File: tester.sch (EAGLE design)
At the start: 74 parts, among them IC1 ATmega8/88/168, K1 NA 05W K, M1 SP6000C-180, P1 250, P2 10k lin, Q1 BC847CSMD, Q2 BC847CSMD, Q3 BC807-40SMD, Q4 8,000 MHz, Q5 BC847CSMD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

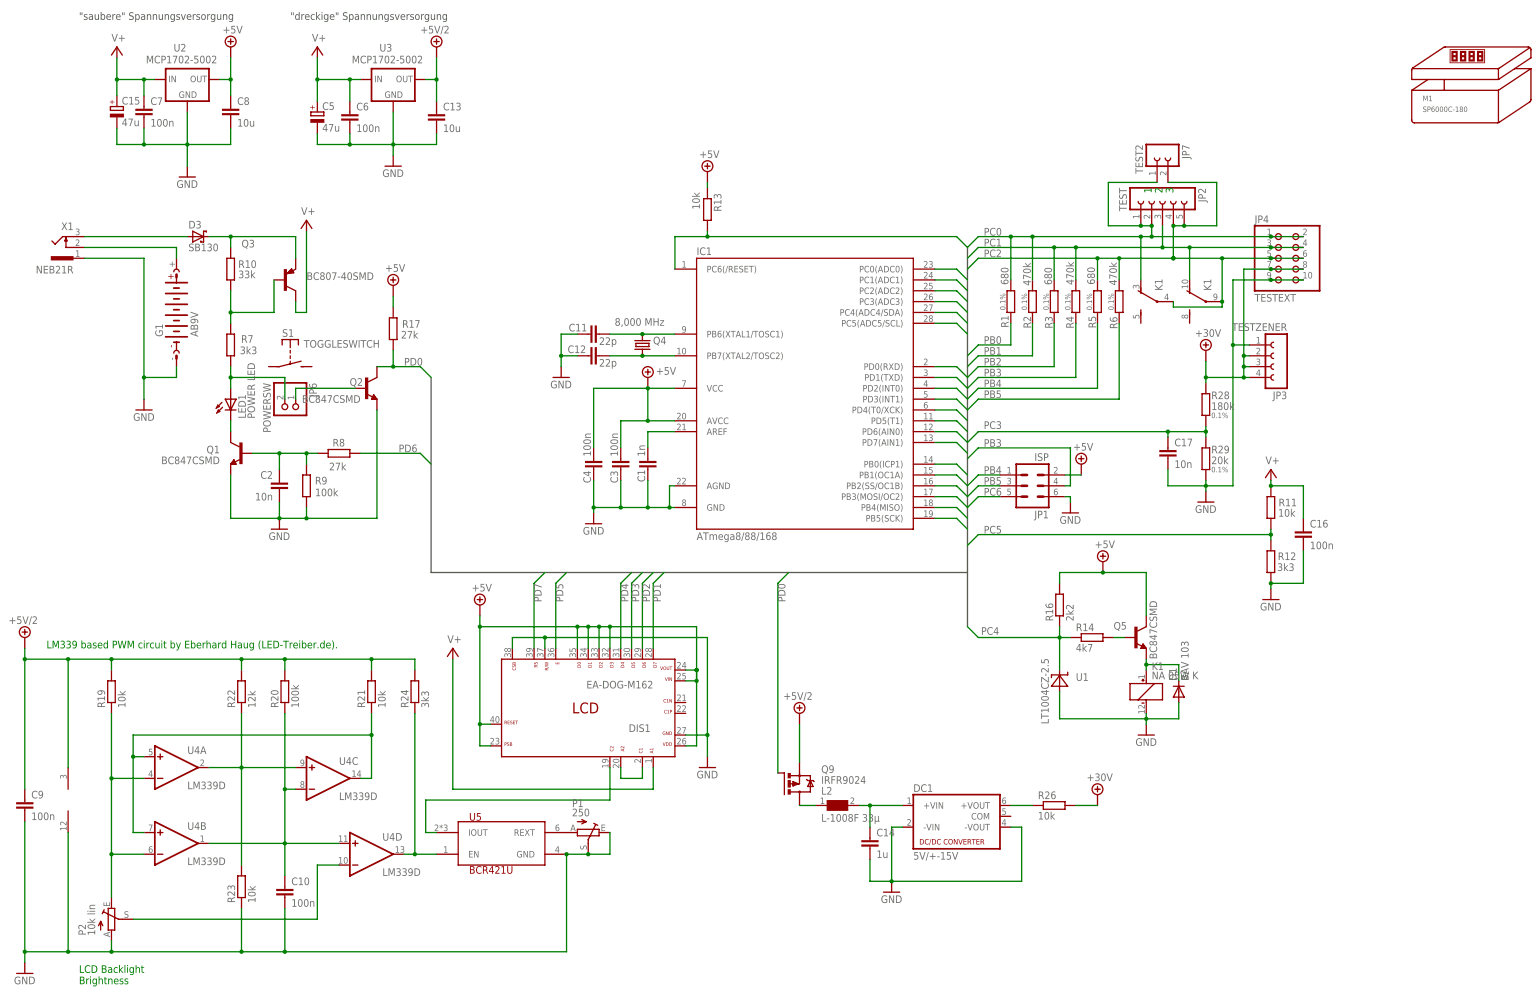
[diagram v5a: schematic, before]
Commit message: adjusted 1702 filter caps
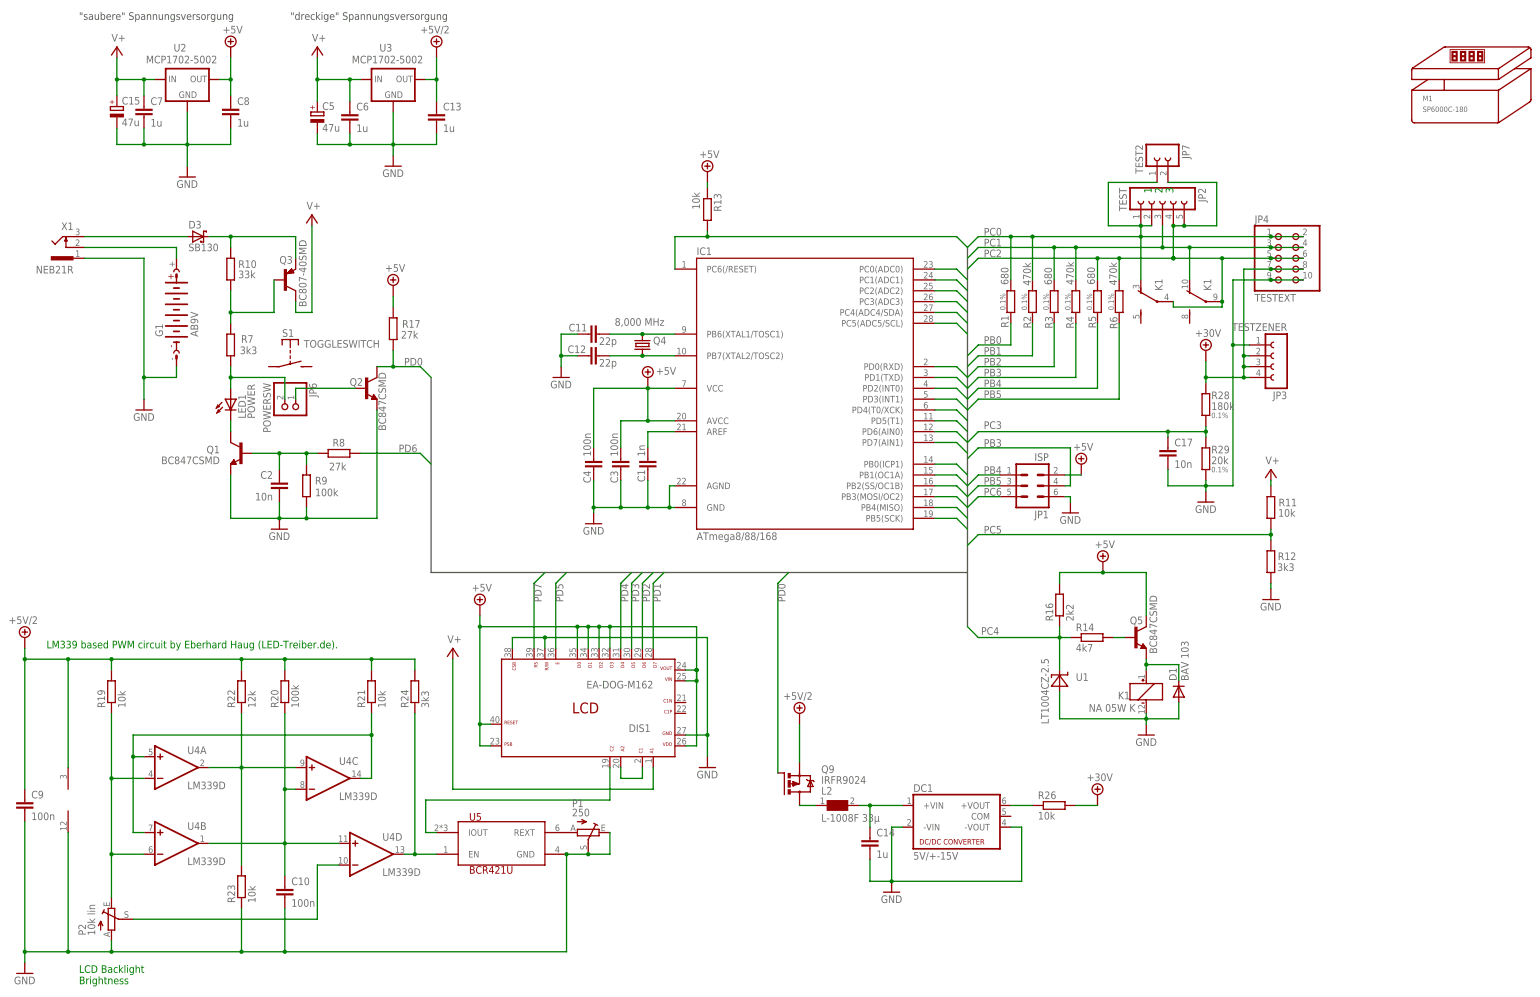
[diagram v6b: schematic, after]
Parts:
- removed C16: 100n, rcl:C-EUC0603
- C13, C8: value 10u -> 1u
- C6, C7: value 100n -> 1u
- LED1: value POWER LED -> POWER
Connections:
- net GND: no longer C16.2
- net V+: no longer C16.1
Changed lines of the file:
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@@
 <setting verticaltext="up"/>
 </settings>
-<grid distance="1.27" unitdist="mm" unit="mm" style="lines" multiple="1" display="yes" altdistance="635" altunitdist="mic" altunit="mic"/>
+<grid distance="0.1" unitdist="inch" unit="mm" style="lines" multiple="1" display="yes" altdistance="0.01" altunitdist="inch" altunit="mm"/>
 <layers>
 <layer number="1" name="Top" color="4" fill="1" visible="no" active="no"/>
@@
 <part name="Q3" library="transistor-pnp" deviceset="BC807*" device="SMD" technology="-40"/>
 <part name="D3" library="markus" deviceset="SCHOTTKY-DIODE" device="_RAD3-5-A" value="SB130"/>
-<part name="LED1" library="led" deviceset="LED" device="5MMEXT" value="POWER LED"/>
+<part name="LED1" library="led" deviceset="LED" device="5MMEXT" value="POWER"/>
 <part name="G1" library="battery" deviceset="AB9V" device=""/>
 <part name="JP2" library="con-lsta" deviceset="FE05-1" device="" value="TEST"/>
@@
 <part name="GND6" library="supply1" deviceset="GND" device=""/>
 <part name="Q9" library="transistor-power" deviceset="IRF?5305" device="R" value="IRFR9024"/>
-<part name="C6" library="rcl" deviceset="C-EU" device="C0603" value="100n"/>
-<part name="C13" library="rcl" deviceset="C-EU" device="C0603" value="10u"/>
+<part name="C6" library="rcl" deviceset="C-EU" device="C0603" value="1u"/>
+<part name="C13" library="rcl" deviceset="C-EU" device="C0603" value="1u"/>
 <part name="C14" library="rcl" deviceset="C-EU" device="C0603" value="1u"/>
 <part name="DC1" library="dc-dc-converter" deviceset="NMA" device="" value="5V/+-15V"/>
@@
 <part name="SUPPLY9" library="supply2" deviceset="V+" device=""/>
 <part name="SUPPLY10" library="supply2" deviceset="V+" device=""/>
-<part name="C7" library="rcl" deviceset="C-EU" device="C0603" value="100n"/>
-<part name="C8" library="rcl" deviceset="C-EU" device="C0603" value="10u"/>
+<part name="C7" library="rcl" deviceset="C-EU" device="C0603" value="1u"/>
+<part name="C8" library="rcl" deviceset="C-EU" device="C0603" value="1u"/>
 <part name="C15" library="rcl" deviceset="CPOL-EU" device="UD-5X5,8" value="47u"/>
 <part name="P1" library="pot" deviceset="TRIM_EU-" device="CA6H" value="250"/>
@@
 <part name="JP7" library="con-lsta" deviceset="FE02-1" device="" value="TEST2"/>
 <part name="SUPPLY5" library="supply2" deviceset="V+" device=""/>
-<part name="C16" library="rcl" deviceset="C-EU" device="C0603" value="100n"/>
 </parts>
 <sheets>
@@
 <instance part="Q2" gate="G$1" x="97.79" y="172.72" smashed="yes">
 <attribute name="NAME" x="93.9292" y="173.3042" size="1.778" layer="95"/>
-<attribute name="VALUE" x="82.7532" y="169.3164" size="1.778" layer="96"/>
+<attribute name="VALUE" x="102.4636" y="162.7632" size="1.778" layer="96" rot="R90"/>
 </instance>
 <instance part="R8" gate="G$1" x="91.44" y="157.48" smashed="yes" rot="MR0">
@@
 <instance part="FRAME1" gate="G$2" x="287.02" y="0"/>
 <instance part="Q3" gate="G$1" x="78.74" y="198.12" smashed="yes">
-<attribute name="NAME" x="68.58" y="205.74" size="1.778" layer="95"/>
-<attribute name="VALUE" x="83.82" y="198.12" size="1.778" layer="96"/>
+<attribute name="NAME" x="77.47" y="201.93" size="1.778" layer="95"/>
+<attribute name="VALUE" x="83.82" y="191.77" size="1.778" layer="96" rot="R90"/>
 </instance>
 <instance part="D3" gate="G$1" x="58.42" y="208.28"/>
@@
 <instance part="GND5" gate="1" x="17.78" y="35.56"/>
 <instance part="P+4" gate="G$1" x="17.78" y="114.3"/>
-<instance part="K1" gate="1" x="280.67" y="101.6"/>
+<instance part="K1" gate="1" x="280.67" y="101.6" smashed="yes">
+<attribute name="VALUE" x="278.13" y="98.679" size="1.778" layer="96" rot="R180"/>
+<attribute name="PART" x="276.86" y="101.6" size="1.778" layer="95" rot="R180"/>
+</instance>
 <instance part="K1" gate="2" x="284.48" y="193.04" rot="R90"/>
 <instance part="K1" gate="3" x="295.91" y="193.04" rot="R90"/>
 <instance part="Q5" gate="G$1" x="278.13" y="114.3" smashed="yes">
-<attribute name="NAME" x="272.9992" y="116.1542" size="1.778" layer="95"/>
-<attribute name="VALUE" x="283.21" y="109.22" size="1.778" layer="96" rot="R90"/>
+<attribute name="NAME" x="276.8092" y="117.4242" size="1.778" layer="95"/>
+<attribute name="VALUE" x="283.21" y="110.49" size="1.778" layer="96" rot="R90"/>
 </instance>
 <instance part="R14" gate="G$1" x="267.97" y="114.3" smashed="yes">
@@
 <instance part="P+5" gate="+5V" x="66.04" y="252.73"/>
 <instance part="GND9" gate="1" x="77.47" y="139.7"/>
-<instance part="SUPPLY4" gate="1" x="83.82" y="212.09"/>
+<instance part="SUPPLY4" gate="1" x="85.09" y="213.36"/>
 <instance part="P+7" gate="+5V" x="163.83" y="175.26" smashed="yes">
 <attribute name="VALUE" x="165.735" y="175.895" size="1.778" layer="96"/>
@@
 <instance part="JP7" gate="G$1" x="284.48" y="228.6" rot="R270"/>
 <instance part="SUPPLY5" gate="1" x="118.11" y="111.76"/>
-<instance part="C16" gate="G$1" x="317.5" y="139.7"/>
 </instances>
 <busses>
@@
 <wire x1="309.88" y1="125.73" x2="309.88" y2="127" width="0.1524" layer="91"/>
 <pinref part="GND11" gate="1" pin="GND"/>
-<pinref part="C16" gate="G$1" pin="2"/>
-<wire x1="309.88" y1="127" x2="317.5" y2="127" width="0.1524" layer="91"/>
-<wire x1="317.5" y1="127" x2="317.5" y2="134.62" width="0.1524" layer="91"/>
-<junction x="309.88" y="127"/>
 </segment>
 <segment>
@@
 <junction x="254" y="208.28"/>
 <pinref part="JP2" gate="G$1" pin="2"/>
-<wire x1="279.4" y1="208.28" x2="281.94" y2="208.28" width="0.1524" layer="91"/>
-<wire x1="281.94" y1="208.28" x2="281.94" y2="210.82" width="0.1524" layer="91"/>
 <wire x1="281.94" y1="210.82" x2="279.4" y2="210.82" width="0.1524" layer="91"/>
-<junction x="281.94" y="210.82"/>
 <pinref part="JP2" gate="G$1" pin="1"/>
-<junction x="281.94" y="208.28"/>
-<wire x1="309.88" y1="208.28" x2="281.94" y2="208.28" width="0.1524" layer="91"/>
+<wire x1="309.88" y1="208.28" x2="279.4" y2="208.28" width="0.1524" layer="91"/>
 <pinref part="JP4" gate="A" pin="1"/>
 <pinref part="K1" gate="2" pin="O"/>
@@
 <pinref part="JP7" gate="G$1" pin="1"/>
 <wire x1="271.78" y1="220.98" x2="283.21" y2="220.98" width="0.1524" layer="91"/>
+<wire x1="279.4" y1="210.82" x2="279.4" y2="208.28" width="0.1524" layer="91"/>
 </segment>
 </net>
@@
 <pinref part="Q3" gate="G$1" pin="C"/>
 <wire x1="81.28" y1="193.04" x2="81.28" y2="190.5" width="0.1524" layer="91"/>
-<wire x1="81.28" y1="190.5" x2="83.82" y2="190.5" width="0.1524" layer="91"/>
-<wire x1="83.82" y1="190.5" x2="83.82" y2="209.55" width="0.1524" layer="91"/>
+<wire x1="81.28" y1="190.5" x2="85.09" y2="190.5" width="0.1524" layer="91"/>
+<wire x1="85.09" y1="190.5" x2="85.09" y2="210.82" width="0.1524" layer="91"/>
 <pinref part="SUPPLY4" gate="1" pin="V+"/>
 </segment>
@@
 <wire x1="309.88" y1="149.86" x2="309.88" y2="151.13" width="0.1524" layer="91"/>
 <pinref part="SUPPLY9" gate="1" pin="V+"/>
-<pinref part="C16" gate="G$1" pin="1"/>
-<wire x1="317.5" y1="142.24" x2="317.5" y2="149.86" width="0.1524" layer="91"/>
-<wire x1="317.5" y1="149.86" x2="309.88" y2="149.86" width="0.1524" layer="91"/>
-<junction x="309.88" y="149.86"/>
-</segment>
-<segment>
+</segment>
+<segment>

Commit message: should know better how to use npn q5
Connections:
- removed net N$23: D1.C, K11.+, Q5.E
- new net N$18: D1.A, K11.-, Q5.C
- net +5V: now also D1.C, K11.+; no longer Q5.C
- net GND: now also Q5.E; no longer D1.A, K11.-
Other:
- moved on the sheet: D1, K1, Q5, R14, U1
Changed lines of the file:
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@@
 <setting verticaltext="up"/>
 </settings>
-<grid distance="0.1" unitdist="inch" unit="mm" style="lines" multiple="1" display="yes" altdistance="0.01" altunitdist="inch" altunit="mm"/>
+<grid distance="1.27" unitdist="mm" unit="mm" style="lines" multiple="1" display="yes" altdistance="635" altunitdist="mic" altunit="mic"/>
 <layers>
 <layer number="1" name="Top" color="4" fill="1" visible="no" active="no"/>
@@
 <part name="JP7" library="con-lsta" deviceset="FE02-1" device="" value="TEST2"/>
 <part name="SUPPLY5" library="supply2" deviceset="V+" device=""/>
+<part name="GND12" library="supply1" deviceset="GND" device=""/>
 </parts>
 <sheets>
@@
 <instance part="GND5" gate="1" x="17.78" y="35.56"/>
 <instance part="P+4" gate="G$1" x="17.78" y="114.3"/>
-<instance part="K1" gate="1" x="280.67" y="101.6" smashed="yes">
-<attribute name="VALUE" x="278.13" y="98.679" size="1.778" layer="96" rot="R180"/>
-<attribute name="PART" x="276.86" y="101.6" size="1.778" layer="95" rot="R180"/>
+<instance part="K1" gate="1" x="274.32" y="114.3" smashed="yes">
+<attribute name="VALUE" x="270.129" y="107.95" size="1.778" layer="96" rot="R90"/>
+<attribute name="PART" x="274.32" y="120.65" size="1.778" layer="95" rot="R180"/>
 </instance>
 <instance part="K1" gate="2" x="284.48" y="193.04" rot="R90"/>
 <instance part="K1" gate="3" x="295.91" y="193.04" rot="R90"/>
-<instance part="Q5" gate="G$1" x="278.13" y="114.3" smashed="yes">
-<attribute name="NAME" x="276.8092" y="117.4242" size="1.778" layer="95"/>
-<attribute name="VALUE" x="283.21" y="110.49" size="1.778" layer="96" rot="R90"/>
-</instance>
-<instance part="R14" gate="G$1" x="267.97" y="114.3" smashed="yes">
-<attribute name="NAME" x="264.16" y="115.7986" size="1.778" layer="95"/>
-<attribute name="VALUE" x="264.16" y="110.998" size="1.778" layer="96"/>
-</instance>
-<instance part="GND4" gate="1" x="280.67" y="91.44"/>
-<instance part="P+8" gate="+5V" x="270.51" y="132.08"/>
+<instance part="Q5" gate="G$1" x="271.78" y="93.98" smashed="yes">
+<attribute name="NAME" x="270.4592" y="97.1042" size="1.778" layer="95"/>
+<attribute name="VALUE" x="276.86" y="90.17" size="1.778" layer="96" rot="R90"/>
+</instance>
+<instance part="R14" gate="G$1" x="260.35" y="93.98" smashed="yes">
+<attribute name="NAME" x="256.54" y="95.4786" size="1.778" layer="95"/>
+<attribute name="VALUE" x="256.54" y="90.678" size="1.778" layer="96"/>
+</instance>
+<instance part="GND4" gate="1" x="260.35" y="102.87"/>
+<instance part="P+8" gate="+5V" x="267.97" y="132.08"/>
 <instance part="R16" gate="G$1" x="260.35" y="121.92" rot="R90"/>
-<instance part="U1" gate="G$1" x="260.35" y="104.14" smashed="yes">
-<attribute name="NAME" x="264.16" y="104.14" size="1.778" layer="95"/>
-<attribute name="VALUE" x="257.81" y="93.98" size="1.778" layer="96" rot="R90"/>
+<instance part="U1" gate="G$1" x="260.35" y="109.22" smashed="yes">
+<attribute name="NAME" x="259.08" y="113.03" size="1.778" layer="95" rot="R180"/>
+<attribute name="VALUE" x="265.43" y="99.06" size="1.778" layer="96" rot="R90"/>
 </instance>
 <instance part="JP4" gate="A" x="312.42" y="203.2">
@@
 <instance part="GND7" gate="1" x="294.64" y="146.05"/>
 <instance part="JP3" gate="G$1" x="312.42" y="179.07" rot="R180"/>
-<instance part="D1" gate="G$1" x="288.29" y="101.6" rot="R90"/>
+<instance part="D1" gate="G$1" x="281.94" y="114.3" rot="R90"/>
 <instance part="U5" gate="G$1" x="129.54" y="66.04"/>
 <instance part="DIS1" gate="G$1" x="149.86" y="99.06" rot="R180"/>
@@
 <instance part="JP7" gate="G$1" x="284.48" y="228.6" rot="R270"/>
 <instance part="SUPPLY5" gate="1" x="118.11" y="111.76"/>
+<instance part="GND12" gate="1" x="274.32" y="85.09"/>
 </instances>
 <busses>
@@
 </segment>
 <segment>
-<pinref part="K1" gate="1" pin="-"/>
 <pinref part="GND4" gate="1" pin="GND"/>
-<wire x1="280.67" y1="96.52" x2="280.67" y2="95.25" width="0.1524" layer="91"/>
-<wire x1="280.67" y1="95.25" x2="280.67" y2="93.98" width="0.1524" layer="91"/>
-<wire x1="280.67" y1="95.25" x2="260.35" y2="95.25" width="0.1524" layer="91"/>
-<junction x="280.67" y="95.25"/>
 <pinref part="U1" gate="G$1" pin="A"/>
-<wire x1="260.35" y1="95.25" x2="260.35" y2="101.6" width="0.1524" layer="91"/>
-<pinref part="D1" gate="G$1" pin="A"/>
-<wire x1="288.29" y1="99.06" x2="288.29" y2="95.25" width="0.1524" layer="91"/>
-<wire x1="288.29" y1="95.25" x2="280.67" y2="95.25" width="0.1524" layer="91"/>
+<wire x1="260.35" y1="105.41" x2="260.35" y2="106.68" width="0.1524" layer="91"/>
 </segment>
 <segment>
@@
 <pinref part="GND3" gate="1" pin="GND"/>
 </segment>
+<segment>
+<pinref part="Q5" gate="G$1" pin="E"/>
+<pinref part="GND12" gate="1" pin="GND"/>
+<wire x1="274.32" y1="87.63" x2="274.32" y2="88.9" width="0.1524" layer="91"/>
+</segment>
 </net>
 <net name="N$5" class="0">
@@
 <segment>
 <pinref part="P+8" gate="+5V" pin="+5V"/>
-<pinref part="Q5" gate="G$1" pin="C"/>
-<wire x1="280.67" y1="129.54" x2="280.67" y2="119.38" width="0.1524" layer="91"/>
-<wire x1="280.67" y1="129.54" x2="270.51" y2="129.54" width="0.1524" layer="91"/>
-<wire x1="270.51" y1="129.54" x2="260.35" y2="129.54" width="0.1524" layer="91"/>
+<wire x1="274.32" y1="129.54" x2="267.97" y2="129.54" width="0.1524" layer="91"/>
+<wire x1="267.97" y1="129.54" x2="260.35" y2="129.54" width="0.1524" layer="91"/>
 <wire x1="260.35" y1="129.54" x2="260.35" y2="127" width="0.1524" layer="91"/>
 <pinref part="R16" gate="G$1" pin="2"/>
-<junction x="270.51" y="129.54"/>
+<junction x="267.97" y="129.54"/>
+<pinref part="K1" gate="1" pin="+"/>
+<pinref part="D1" gate="G$1" pin="C"/>
+<wire x1="274.32" y1="119.38" x2="274.32" y2="121.92" width="0.1524" layer="91"/>
+<wire x1="274.32" y1="121.92" x2="281.94" y2="121.92" width="0.1524" layer="91"/>
+<wire x1="281.94" y1="121.92" x2="281.94" y2="116.84" width="0.1524" layer="91"/>
+<wire x1="274.32" y1="129.54" x2="274.32" y2="121.92" width="0.1524" layer="91"/>
+<junction x="274.32" y="121.92"/>
 </segment>
 <segment>
@@
 <pinref part="U1" gate="G$1" pin="C"/>
 <pinref part="R14" gate="G$1" pin="1"/>
-<wire x1="260.35" y1="114.3" x2="262.89" y2="114.3" width="0.1524" layer="91"/>
+<wire x1="252.73" y1="114.3" x2="252.73" y2="93.98" width="0.1524" layer="91"/>
+<wire x1="252.73" y1="93.98" x2="255.27" y2="93.98" width="0.1524" layer="91"/>
 <pinref part="R16" gate="G$1" pin="1"/>
 <wire x1="260.35" y1="116.84" x2="260.35" y2="114.3" width="0.1524" layer="91"/>
-<wire x1="260.35" y1="114.3" x2="260.35" y2="106.68" width="0.1524" layer="91"/>
+<wire x1="252.73" y1="114.3" x2="260.35" y2="114.3" width="0.1524" layer="91"/>
+<junction x="252.73" y="114.3"/>
+<wire x1="260.35" y1="114.3" x2="260.35" y2="111.76" width="0.1524" layer="91"/>
+<wire x1="238.76" y1="116.84" x2="241.3" y2="114.3" width="0.1524" layer="91"/>
+<wire x1="241.3" y1="114.3" x2="252.73" y2="114.3" width="0.1524" layer="91"/>
+<label x="241.935" y="114.935" size="1.778" layer="95"/>
 <junction x="260.35" y="114.3"/>
-<wire x1="238.76" y1="116.84" x2="241.3" y2="114.3" width="0.1524" layer="91"/>
-<wire x1="241.3" y1="114.3" x2="260.35" y2="114.3" width="0.1524" layer="91"/>
-<label x="241.935" y="114.935" size="1.778" layer="95"/>
 </segment>
 <segment>
@@
 <pinref part="R14" gate="G$1" pin="2"/>
 <pinref part="Q5" gate="G$1" pin="B"/>
-<wire x1="273.05" y1="114.3" x2="275.59" y2="114.3" width="0.1524" layer="91"/>
-</segment>
-</net>
-<net name="N$23" class="0">
-<segment>
-<pinref part="Q5" gate="G$1" pin="E"/>
-<pinref part="K1" gate="1" pin="+"/>
-<wire x1="280.67" y1="109.22" x2="280.67" y2="107.95" width="0.1524" layer="91"/>
-<pinref part="D1" gate="G$1" pin="C"/>
-<wire x1="280.67" y1="107.95" x2="280.67" y2="106.68" width="0.1524" layer="91"/>
-<wire x1="288.29" y1="104.14" x2="288.29" y2="107.95" width="0.1524" layer="91"/>
-<wire x1="280.67" y1="107.95" x2="288.29" y2="107.95" width="0.1524" layer="91"/>
-<junction x="280.67" y="107.95"/>
+<wire x1="269.24" y1="93.98" x2="265.43" y2="93.98" width="0.1524" layer="91"/>
 </segment>
 </net>
@@
 </segment>
 </net>
+<net name="N$18" class="0">
+<segment>
+<pinref part="Q5" gate="G$1" pin="C"/>
+<pinref part="K1" gate="1" pin="-"/>
+<wire x1="274.32" y1="99.06" x2="274.32" y2="106.68" width="0.1524" layer="91"/>
+<pinref part="D1" gate="G$1" pin="A"/>
+<wire x1="274.32" y1="106.68" x2="274.32" y2="109.22" width="0.1524" layer="91"/>
+<wire x1="274.32" y1="106.68" x2="281.94" y2="106.68" width="0.1524" layer="91"/>
+<wire x1="281.94" y1="106.68" x2="281.94" y2="111.76" width="0.1524" layer="91"/>
+<junction x="274.32" y="106.68"/>
+</segment>
+</net>
